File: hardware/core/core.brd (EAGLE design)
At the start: 159.7 x 163.8 mm, 520 parts, among them IC1 MAX481CSA, IC10 MAX481CSA, IC11 MAX481CSA, IC12 MAX481CSA, IC13 MAX481CSA, IC14 MAX481CSA, IC15 MAX481CSA, IC16 MAX481CSA, IC17 MAX481CSA, IC18 MAX481CSA, IC19 MAX481CSA, IC2 LD117AS12TR, IC20 MAX481CSA, IC21 MAX481CSA, IC22 LD117AS12TR, IC23 LD117AS12TR, IC3 MAX481CSA, IC4 MAX481CSA, IC5 MAX481CSA, IC6 MAX481CSA, IC7 MAX481CSA, IC8 MAX481CSA, IC9 MAX481CSA

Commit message: Fix for button status resistors & 12v status dim
Fix for button status resistors & 12v status dim
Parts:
- added R220, R223: R_270R_0603, JLC PCB Basic Parts_loc:R0603
- added R221, R222: R_56R_0603, JLC PCB Basic Parts_loc:R0603
- added R224: R_82R_0603, JLC PCB Basic Parts_loc:R0603
- R132: value 12k -> R_1.8K_0603; device rcl:R0603 -> JLC PCB Basic Parts_loc:R0603
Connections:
- new net N$320: D86.A, R220.2
- new net N$321: D87.A, R221.2
- new net N$322: D88.A, R222.2
- new net N$323: D90.A, R223.2
- new net N$324: D89.A, R224.2
- net +3V3: now also R220.1, R221.1, R222.1, R223.1, R224.1; no longer D86.A, D87.A, D88.A, D89.A, D90.A
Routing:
- net +5V: track 935.7 -> 0.00 mm, vias 9 -> 0
- net +3V3: track 926.9 -> 0.00 mm, vias 7 -> 0
- net GND: track 836.8 -> 0.00 mm, vias 77 -> 0
- net +12V: track 614.6 -> 0.00 mm, vias 3 -> 0
- net 13: track 454.0 -> 0.00 mm, vias 21 -> 0
- net 16: track 413.4 -> 0.00 mm, vias 8 -> 0
- net 17: track 409.2 -> 0.00 mm, vias 21 -> 0
- net 22/SCL: track 329.5 -> 0.00 mm, vias 9 -> 0
- net 21/SDA: track 315.1 -> 0.00 mm, vias 8 -> 0
- net H10: track 225.2 -> 0.00 mm, vias 1 -> 0
- net H11: track 218.3 -> 0.00 mm, vias 1 -> 0
- net H9: track 209.8 -> 0.00 mm, vias 5 -> 0
- net H12: track 196.2 -> 0.00 mm, vias 1 -> 0
- net 4: track 195.8 -> 0.00 mm, vias 1 -> 0
- net H8: track 195.2 -> 0.00 mm, vias 4 -> 0
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
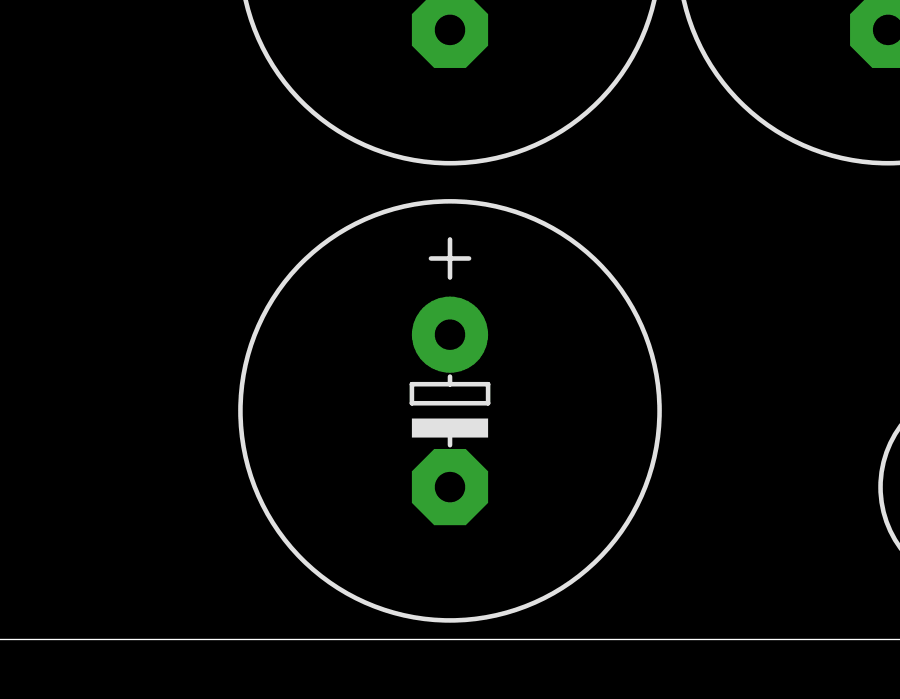
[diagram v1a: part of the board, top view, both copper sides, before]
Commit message: Updated bulk capacitor spacing
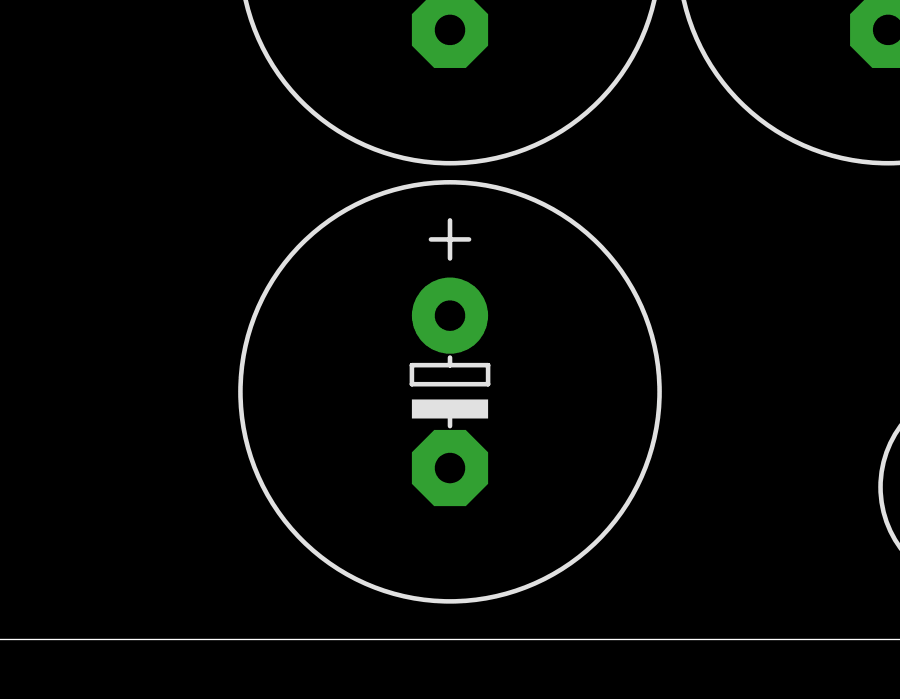
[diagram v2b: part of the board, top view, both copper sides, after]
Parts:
- moved C89 0.64 mm to (137.2, 8.26)
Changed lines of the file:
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@@
 <layers>
 <layer number="1" name="Top" color="4" fill="1" visible="yes" active="yes"/>
-<layer number="2" name="$GND" color="16" fill="10" visible="yes" active="yes"/>
+<layer number="2" name="$GND" color="16" fill="10" visible="no" active="yes"/>
 <layer number="3" name="Route3" color="17" fill="1" visible="no" active="no"/>
 <layer number="4" name="Route4" color="18" fill="1" visible="no" active="no"/>
@@
 <attribute name="SPICEPREFIX" value="C" x="69.85" y="119.38" size="1.778" layer="27" rot="R270" display="off"/>
 </element>
-<element name="C89" library="rcl" library_urn="urn:adsk.eagle:library:334" package="E5-13" package3d_urn="urn:adsk.eagle:package:23375/1" value="2200uf" x="137.16" y="7.62" smashed="yes" rot="R270">
-<attribute name="DIST" value="https://amzn.to/3iR84VS" x="137.16" y="7.62" size="1.778" layer="27" rot="R270" display="off"/>
-<attribute name="POPULARITY" value="7" x="137.16" y="7.62" size="1.778" layer="27" rot="R270" display="off"/>
-<attribute name="SPICEPREFIX" value="C" x="137.16" y="7.62" size="1.778" layer="27" rot="R270" display="off"/>
-<attribute name="VALUE" x="133.223" y="12.192" size="1.778" layer="27" ratio="10" rot="R270"/>
+<element name="C89" library="rcl" library_urn="urn:adsk.eagle:library:334" package="E5-13" package3d_urn="urn:adsk.eagle:package:23375/1" value="2200uf" x="137.16" y="8.255" smashed="yes" rot="R270">
+<attribute name="DIST" value="https://amzn.to/3iR84VS" x="137.16" y="8.255" size="1.778" layer="27" rot="R270" display="off"/>
+<attribute name="POPULARITY" value="7" x="137.16" y="8.255" size="1.778" layer="27" rot="R270" display="off"/>
+<attribute name="SPICEPREFIX" value="C" x="137.16" y="8.255" size="1.778" layer="27" rot="R270" display="off"/>
+<attribute name="VALUE" x="133.223" y="12.827" size="1.778" layer="27" ratio="10" rot="R270"/>
 </element>
 <element name="R188" library="rcl" library_urn="urn:adsk.eagle:library:334" package="R0603" package3d_urn="urn:adsk.eagle:package:23555/3" value="68" x="63.5" y="137.795" smashed="yes" rot="R90">
@@
 <wire x1="102.21" y1="18.81" x2="99.91" y2="21.59" width="0" layer="19" extent="1-1"/>
 <wire x1="97.8111" y1="5.055" x2="102.21" y2="18.81" width="0" layer="19" extent="1-1"/>
-<wire x1="137.16" y1="10.16" x2="102.21" y2="18.81" width="0" layer="19" extent="1-1"/>
+<wire x1="137.16" y1="10.795" x2="102.21" y2="18.81" width="0" layer="19" extent="1-1"/>
 <wire x1="82.12" y1="160.02" x2="75.565" y2="101.4222" width="0" layer="19" extent="1-1"/>
 <wire x1="21.197" y1="4.445" x2="89.75" y2="21.59" width="0" layer="19" extent="1-1"/>
